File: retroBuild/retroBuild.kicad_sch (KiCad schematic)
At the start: 21 parts, among them J1 AVR-ISP-6, SW1 SW_push_reset, U1 PRTR5V0U2X, U2 ATmega32U4-A, Y1 Crystal_GND24_Small

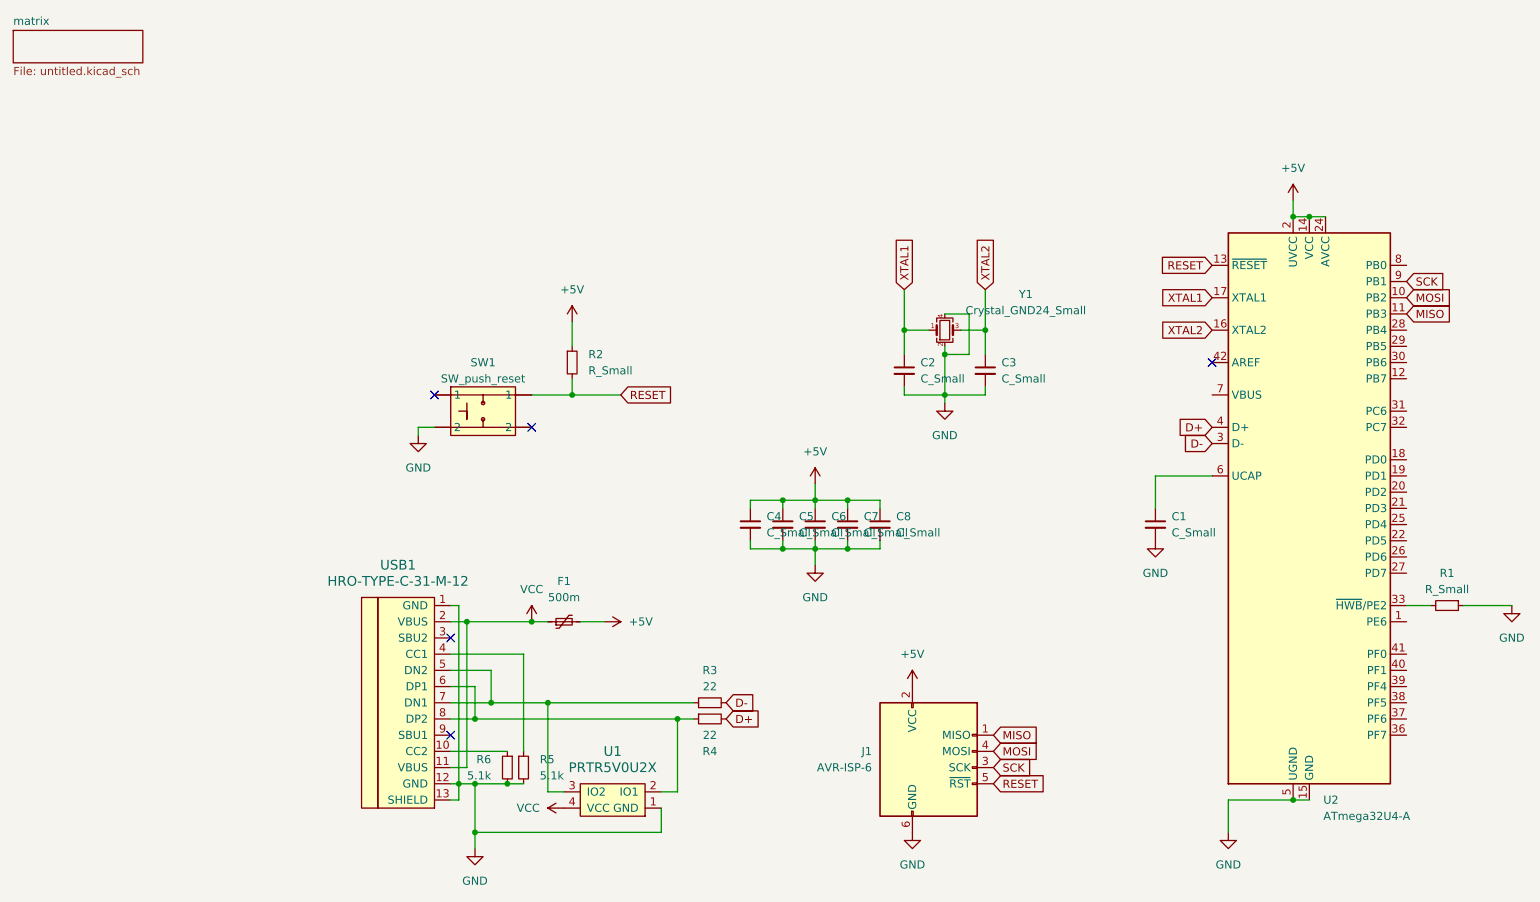
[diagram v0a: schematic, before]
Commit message: keys layed out in pcb view
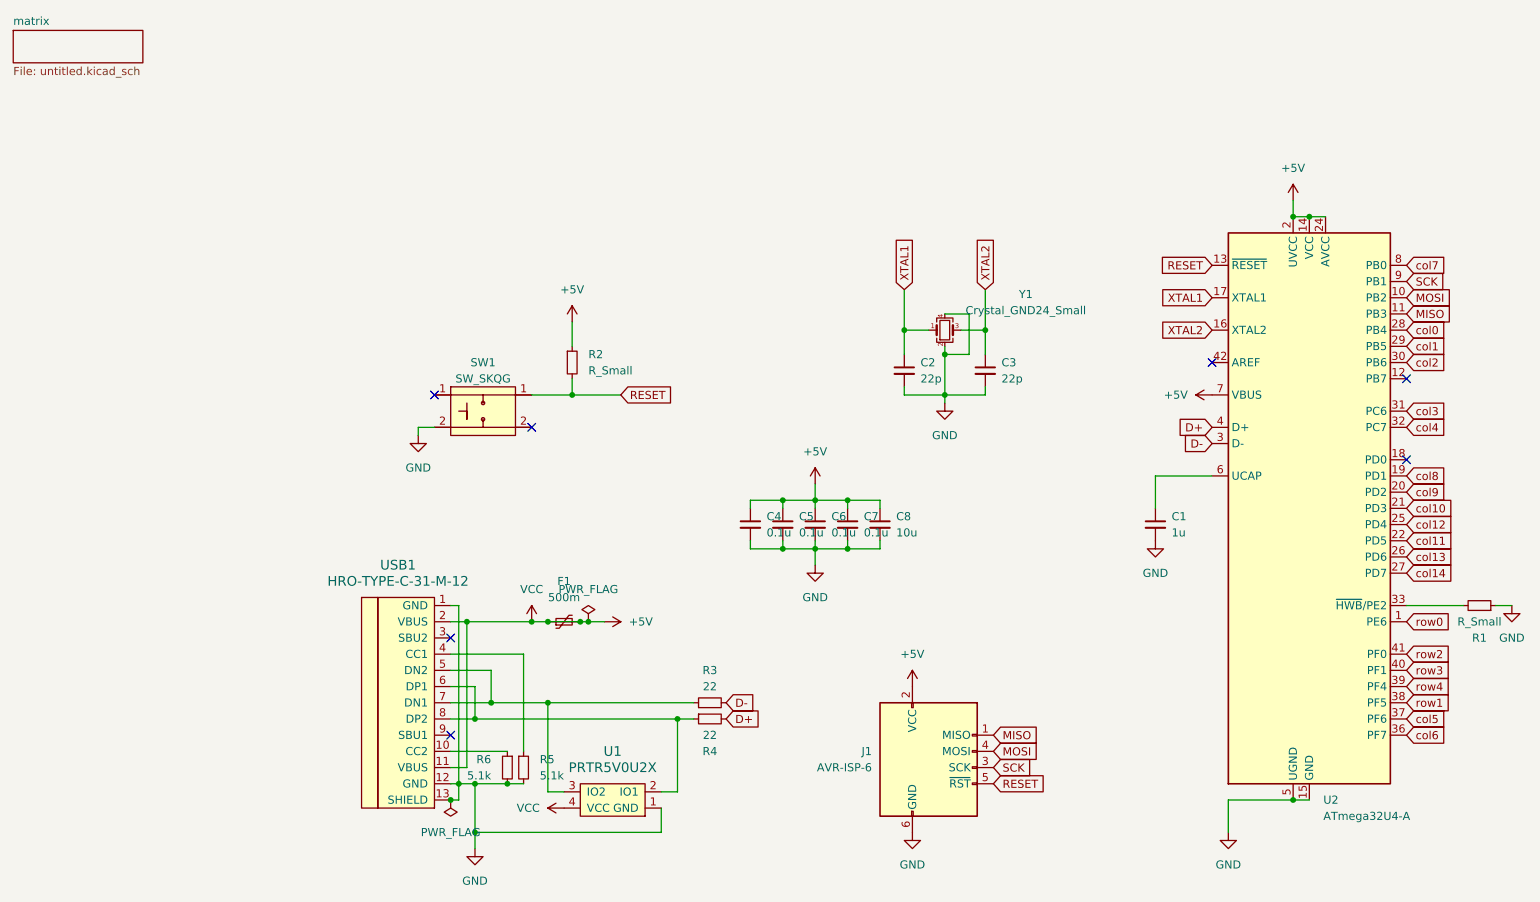
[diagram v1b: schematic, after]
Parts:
- C1: value C_Small -> 1u; footprint (none) -> Capacitor_SMD:C_0805_2012Metric_Pad1.18x1.45mm_HandSolder
- C2, C3: value C_Small -> 22p; footprint (none) -> Capacitor_SMD:C_0805_2012Metric_Pad1.18x1.45mm_HandSolder
- C4, C5, C6, C7: value C_Small -> 0.1u; footprint (none) -> Capacitor_SMD:C_0805_2012Metric_Pad1.18x1.45mm_HandSolder
- C8: value C_Small -> 10u; footprint (none) -> Capacitor_SMD:C_0805_2012Metric_Pad1.18x1.45mm_HandSolder
- F1: footprint (none) -> Fuse:Fuse_1206_3216Metric_Pad1.42x1.75mm_HandSolder
- J1: footprint (none) -> random-keyboard-parts.pretty-master:Reset_Pretty-Mask
- R1, R2, R3, R4, R5, R6: footprint (none) -> Resistor_SMD:R_0805_2012Metric_Pad1.20x1.40mm_HandSolder
- SW1: value SW_push_reset -> SW_SKQG; footprint (none) -> Button_Switch_SMD:SW_SPST_SKQG_WithStem
- U1: footprint (none) -> random-keyboard-parts.pretty-master:SOT143B
- USB1: footprint (none) -> Type-C.pretty-master:HRO-TYPE-C-31-M-12-HandSoldering
- Y1: footprint (none) -> Crystal:Crystal_SMD_3225-4Pin_3.2x2.5mm_HandSoldering
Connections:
- net VCC is gone; now on net +5V: F1.1, U1.4 (VCC), USB1.11 (VBUS), USB1.2 (VBUS)
- net +5V: now also U2.7 (VBUS)
- net GND: now also SW1.2; no longer SW1. (2)
- net RESET: now also SW1.1; no longer SW1. (2)
- net row0: now reaches U2.1 (PE6)
- net col8: now reaches U2.19 (PD1)
- net col9: now reaches U2.20 (PD2)
- net col10: now reaches U2.21 (PD3)
- net col11: now reaches U2.22 (PD5)
- net col12: now reaches U2.25 (PD4)
- net col13: now reaches U2.26 (PD6)
- net col14: now reaches U2.27 (PD7)
- net col0: now reaches U2.28 (PB4)
- net col1: now reaches U2.29 (PB5)
- net col2: now reaches U2.30 (PB6)
- net col3: now reaches U2.31 (PC6)
- net col4: now reaches U2.32 (PC7)
- net col6: now reaches U2.36 (PF7)
- net col5: now reaches U2.37 (PF6)
- net row1: now reaches U2.38 (PF5)
- net row4: now reaches U2.39 (PF4)
- net row3: now reaches U2.40 (PF1)
- net row2: now reaches U2.41 (PF0)
- net col7: now reaches U2.8 (PB0)
- no-connect marks 5 -> 7
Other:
- moved on the sheet: R1
